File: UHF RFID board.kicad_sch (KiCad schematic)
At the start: 29 parts, among them J1 FZ_full_module, J2 picoblade, J4 ICSP, J5 SPI, U1 YRM1001, U2 SEC1210

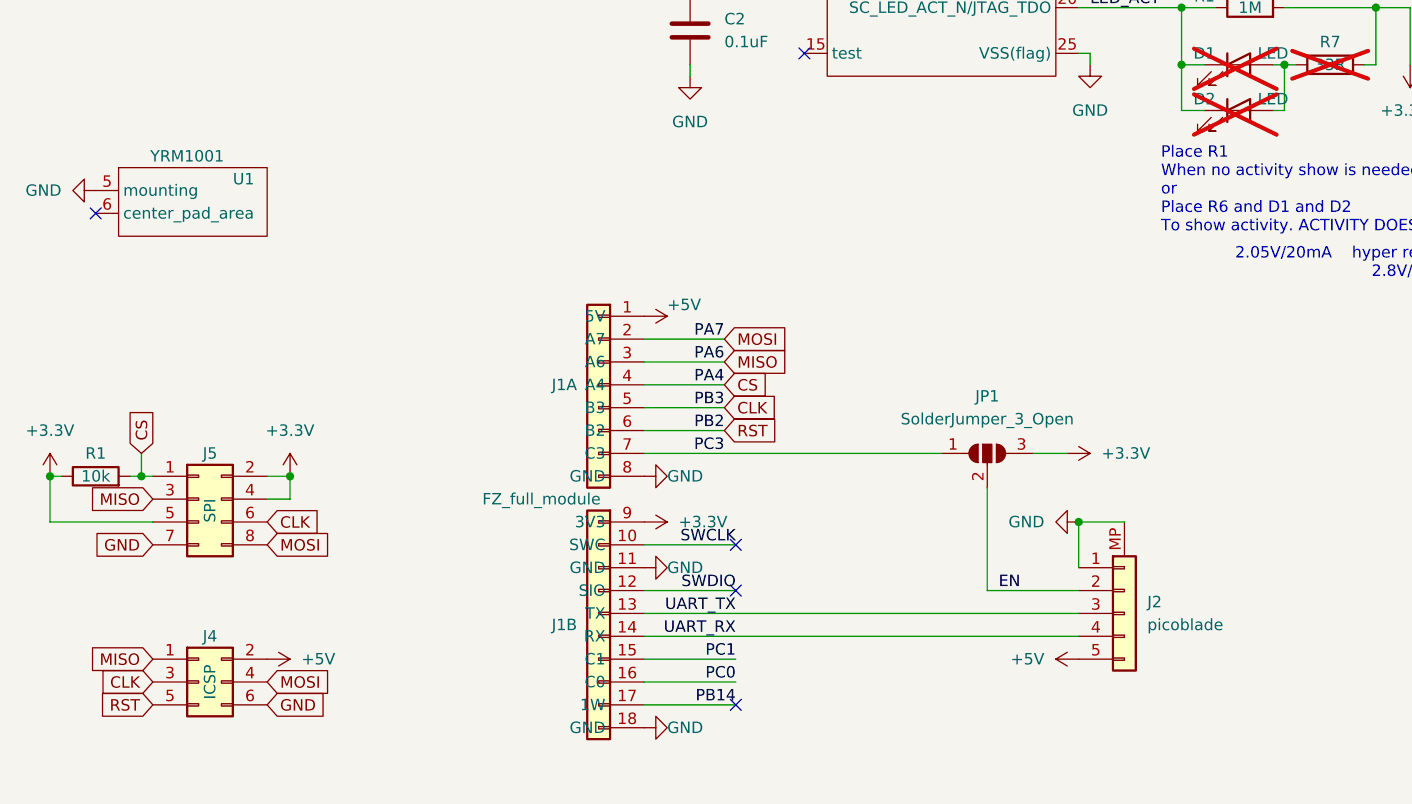
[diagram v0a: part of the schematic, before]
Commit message: V2.6.0
- flipped the inputs of the picoblade connector, so there's no longer a need for a pass-through cable which in hindsight, good. it seemed dumb a long time ago, but you live and learn. Now the off-the shelf cable from Molex (P/N: 151340500) will work as-is, no rewiring needed.
- nudged the whole SAM stuff 1mm higher, which should no longer hinder connecting/disconnecting the picoblade cable in some cases.
(previously if a SIM slot was soldered in CARD 2, the connector would barely hit the end of the SIM slot. Now it doesn't.)
- updated board version number to V2.6.0
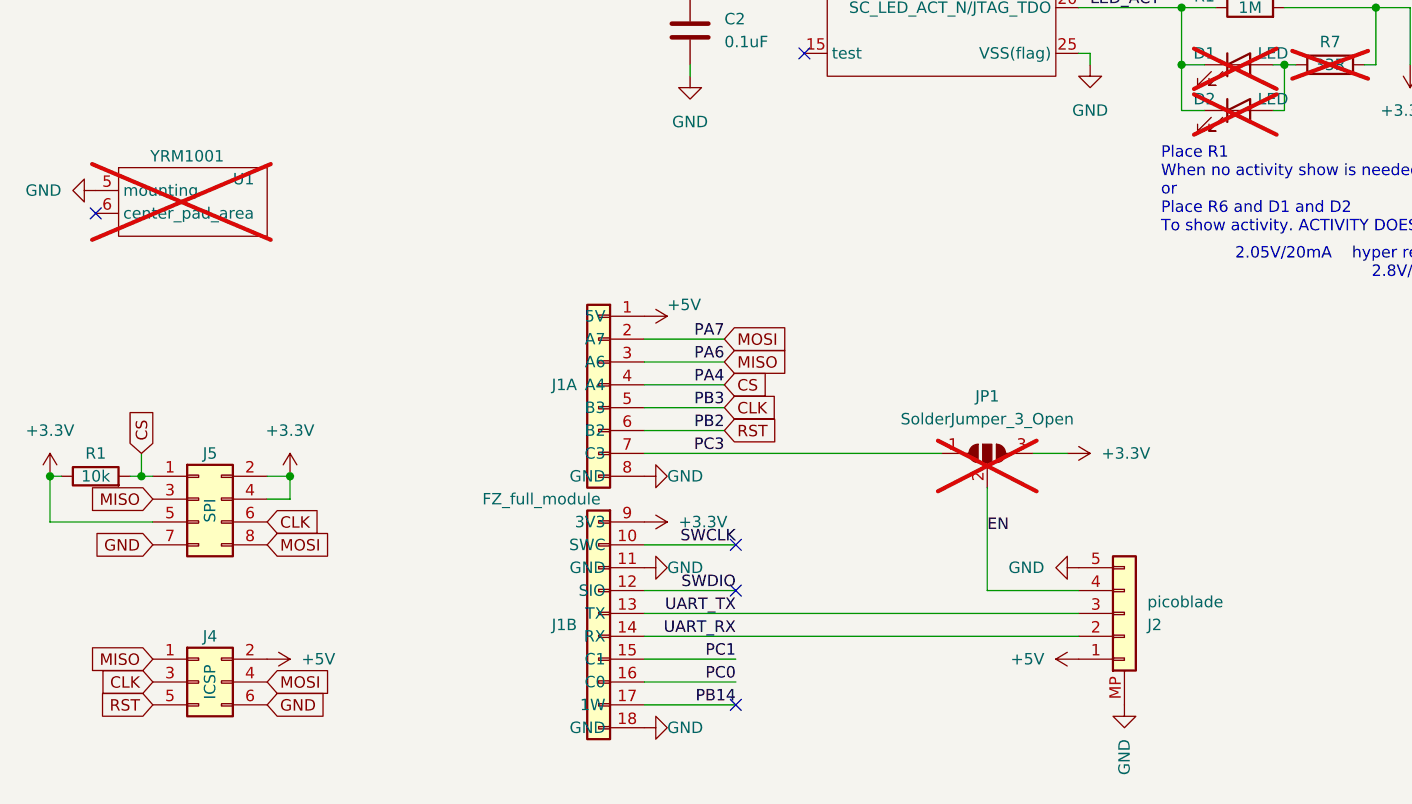
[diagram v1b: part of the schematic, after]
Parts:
- JP1, U1: now not fitted
- R1: mouser (none) -> https://www.mouser.fr/ProductDetail/652-CR0402FX-1004GLF
- R3, R5: mouser https://www.mouser.fr/ProductDetail/?qs=ePR1ZvdkOKKmGsQnUAr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 -> https://www.mouser.fr/ProductDetail/Bourns/CR0402-FX-43R0GL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
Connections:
- net +5V: now also J2.1 (Pin_1); no longer J2.5 (Pin_5)
- net EN: now also J2.4 (Pin_4); no longer J2.2 (Pin_2)
- net GND: now also J2.5 (Pin_5); no longer J2.1 (Pin_1)
- net UART_RX: now also J2.2 (Pin_2); no longer J2.4 (Pin_4)
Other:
- moved on the sheet: J2
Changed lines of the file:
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@@
 	)
 	(junction
-		(at 135.89 165.1)
-		(diameter 0)
-		(color 0 0 0 0)
-	)
-	(junction
 		(at 167.64 46.99)
 		(diameter 0)
@@
 	(wire
 		(pts
+			(xy 125.73 172.72) (xy 135.89 172.72)
+		)
+		(stroke
+			(width 0)
+			(type default)
+		)
+	)
+	(wire
+		(pts
 			(xy 195.58 81.28) (xy 193.04 81.28)
 		)
@@
 	(wire
 		(pts
-			(xy 135.89 165.1) (xy 140.97 165.1)
-		)
-		(stroke
-			(width 0)
-			(type default)
-		)
-	)
-	(wire
-		(pts
 			(xy 171.45 69.85) (xy 180.34 69.85)
 		)
@@
 	(wire
 		(pts
-			(xy 125.73 161.29) (xy 125.73 172.72)
-		)
-		(stroke
-			(width 0)
-			(type default)
-		)
-	)
-	(wire
-		(pts
 			(xy 229.87 46.99) (xy 238.76 46.99)
 		)
@@
 	(wire
 		(pts
-			(xy 135.89 172.72) (xy 125.73 172.72)
-		)
-		(stroke
-			(width 0)
-			(type default)
-		)
-	)
-	(wire
-		(pts
 			(xy 87.63 185.42) (xy 97.79 185.42)
 		)
@@
 	(wire
 		(pts
+			(xy 125.73 161.29) (xy 125.73 172.72)
+		)
+		(stroke
+			(width 0)
+			(type default)
+		)
+	)
+	(wire
+		(pts
 			(xy 236.22 49.53) (xy 236.22 62.23)
 		)
@@
 	(wire
 		(pts
-			(xy 135.89 170.18) (xy 135.89 165.1)
-		)
-		(stroke
-			(width 0)
-			(type default)
-		)
-	)
-	(wire
-		(pts
 			(xy 31.75 160.02) (xy 31.75 157.48)
 		)
@@
 	)
 	(label "EN"
-		(at 127 172.72 0)
+		(at 125.73 166.37 0)
 		(fields_autoplaced yes)
 		(effects
@@
 		(in_bom yes)
 		(on_board yes)
-		(dnp no)
+		(dnp yes)
 		(fields_autoplaced yes)
 		(property "Reference" "JP1"
@@
 			)
 		)
-		(property "mouser" "https://www.mouser.fr/ProductDetail/?qs=ePR1ZvdkOKKmGsQnUArpPA%3D%3D"
+		(property "mouser" "https://www.mouser.fr/ProductDetail/Bourns/CR0402-FX-43R0GLF?qs=ePR1ZvdkOKKmGsQnUArpPA%3D%3D"
 			(at 146.05 77.47 0)
 			(effects
@@
 	(symbol
 		(lib_id "power:GND")
-		(at 135.89 165.1 270)
+		(at 135.89 170.18 270)
 		(unit 1)
 		(exclude_from_sim no)
@@
 		(dnp no)
 		(property "Reference" "#PWR08"
-			(at 129.54 165.1 0)
+			(at 129.54 170.18 0)
 			(effects
 				(font
@@
 		)
 		(property "Value" "GND"
-			(at 132.08 165.1 90)
+			(at 132.08 170.18 90)
 			(effects
 				(font
@@
 		)
 		(property "Footprint" ""
-			(at 135.89 165.1 0)
+			(at 135.89 170.18 0)
 			(effects
 				(font
@@
 		)
 		(property "Datasheet" ""
-			(at 135.89 165.1 0)
+			(at 135.89 170.18 0)
 			(effects
 				(font
@@
 		)
 		(property "Description" ""
-			(at 135.89 165.1 0)
+			(at 135.89 170.18 0)
 			(effects
 				(font
@@
 		(in_bom yes)
 		(on_board yes)
-		(dnp no)
+		(dnp yes)
 		(property "Reference" "U1"
 			(at 41.91 127 0)
@@
 			)
 		)
-		(property "mouser" "https://www.mouser.fr/ProductDetail/?qs=ePR1ZvdkOKKmGsQnUArpPA%3D%3D"
+		(property "mouser" "https://www.mouser.fr/ProductDetail/Bourns/CR0402-FX-43R0GLF?qs=ePR1ZvdkOKKmGsQnUArpPA%3D%3D"
 			(at 144.78 54.61 90)
 			(effects
@@
 			)
 		)
-		(property "Datasheet" "DNP"
+		(property "Datasheet" "~"
 			(at 154.94 107.95 0)
 			(effects
@@
 			)
 		)
-		(property "mouser" ""
+		(property "mouser" "https://www.mouser.fr/ProductDetail/652-CR0402FX-1004GLF"
 			(at 154.94 107.95 0)
 			(effects
@@
 	)
 	(symbol
+		(lib_id "power:GND")
+		(at 140.97 185.42 0)
+		(unit 1)
+		(exclude_from_sim no)
+		(in_bom yes)
+		(on_board yes)
+		(dnp no)
+		(property "Reference" "#PWR019"
+			(at 140.97 191.77 0)
+			(effects
+				(font
+					(size 1.27 1.27)
+				)
+				(hide yes)
+			)
+		)
+		(property "Value" "GND"
+			(at 140.97 189.23 90)
+			(effects
+				(font
+					(size 1.27 1.27)
+				)
+				(justify right)
+			)
+		)
+		(property "Footprint" ""
+			(at 140.97 185.42 0)
+			(effects
+				(font
+					(size 1.27 1.27)
+				)
+				(hide yes)
+			)
+		)
+		(property "Datasheet" ""
+			(at 140.97 185.42 0)
+			(effects
+				(font
+					(size 1.27 1.27)
+				)
+				(hide yes)
+			)
+		)
+		(property "Description" ""
+			(at 140.97 185.42 0)
+			(effects
+				(font
+					(size 1.27 1.27)
+				)
+				(hide yes)
+			)
+		)
+		(pin "1"
+		)
+		(instances
+			(project "UHF RFID board"
+				(path "/d8d0a45f-1f46-4ba4-9944-4b3c9d150d73"
+					(reference "#PWR019")
+					(unit 1)
+				)
+			)
+		)
+	)
+	(symbol
 		(lib_id "custom symbols:SIM_Card_slot")
 		(at 251.46 77.47 0)
@@
 		(lib_id "Connector_Generic:Conn_01x05")
 		(at 140.97 175.26 0)
+		(mirror x)
 		(unit 1)
 		(exclude_from_sim no)
@@
 		(dnp no)
 		(property "Reference" "J2"
-			(at 143.51 173.99 0)
+			(at 143.51 176.53 0)
 			(effects
 				(font
@@
 		)
 		(property "Value" "picoblade"
-			(at 143.51 176.53 0)
+			(at 143.51 173.99 0)
 			(effects
 				(font
